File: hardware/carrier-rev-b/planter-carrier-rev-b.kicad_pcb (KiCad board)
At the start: 2 copper layers, 50.1 x 32.6 mm, 24 parts, among them J1 PROTECTED BATTERY, J2 MOISTURE PROBE, J3 WEACT 1.54 INCH, J4 XIAO BAT LEADS, Q1 AO3401A, U1 Seeed XIAO ESP32-C6 or ESP32-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

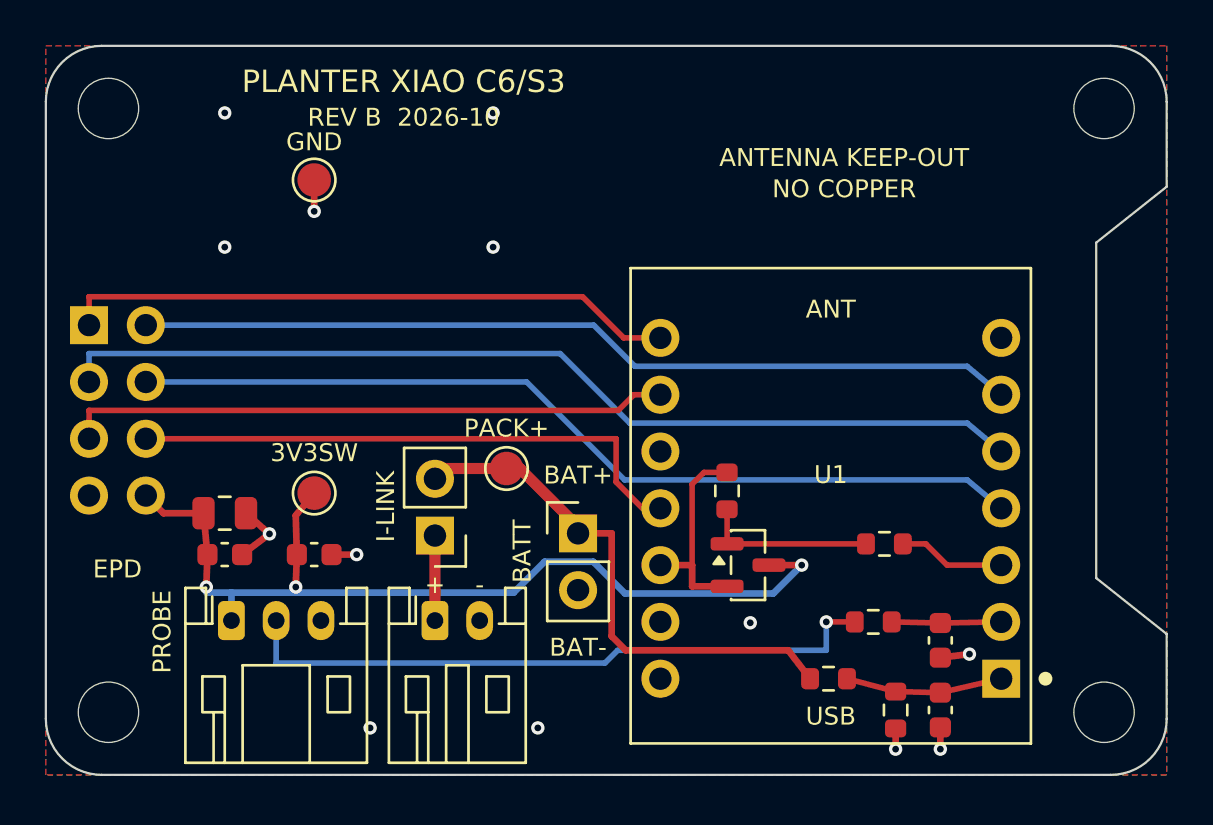
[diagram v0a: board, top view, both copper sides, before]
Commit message: Rev B carrier: freeze on XIAO ESP32-S3, soldered flat
The socketed C6-or-S3 layout left the XIAO's underside BAT pads to a
flying lead that had to leave the socket tunnel and loop back to J4, and
the module could only sit on headers above the passives. With one chip
the board can use its exact land pattern instead.

- U1 is Seeed's XIAO-ESP32-S3-SMD land pattern, rotated so USB-C stays
  at the bottom edge. The underside BAT+/BAT- pads land on plated pads
  (solder from the back, or reflow); J4 is gone.
- Nothing sits under the module. The S3 uses a U.FL antenna, so the C6
  antenna keep-out is dropped: the XIAO moves left beside J3 and the
  switch, divider and filters use the freed right side and top band.
- Pin map rearranged for the layout (display on the left-row pins, D6/TX
  unconnected); firmware Rev B map and platformio-rev-b.ini follow, and
  the C6 env is removed.
- Generators find KiCad on Linux as well as macOS. check.sh passes on
  KiCad 10.0.7: ERC, DRC and parity clean.

Co-Authored-By: Claude Opus 5.5 <noreply@anthropic.com>
Claude-Session: https://claude.ai/code/session_01Y2pFZDRMef9EECGaLGphfU
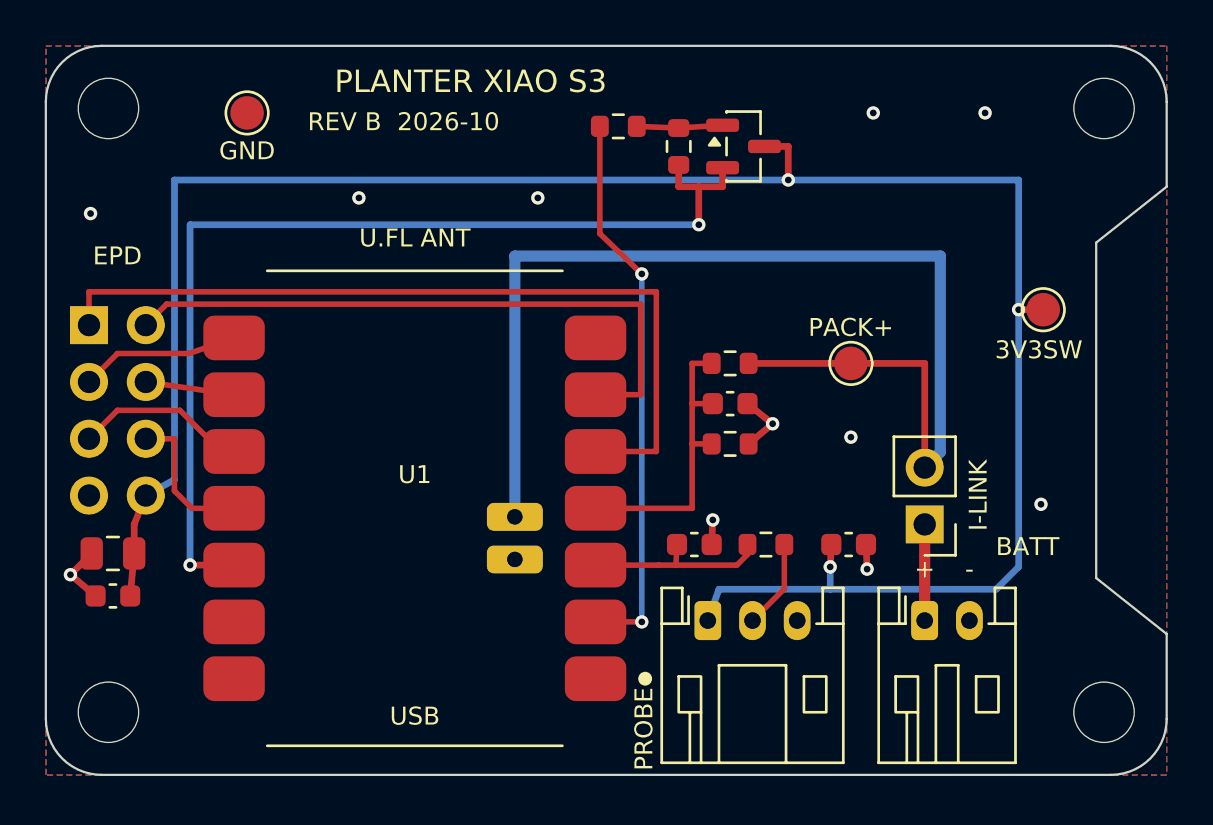
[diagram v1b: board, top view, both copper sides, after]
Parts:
- removed J4: XIAO BAT LEADS, Connector_PinHeader_2.54mm:PinHeader_1x02_P2.54mm_Vertical
- U1: value Seeed XIAO ESP32-C6 or ESP32-S3 -> Seeed XIAO ESP32-S3; footprint Planter:Seeed_XIAO_Socketed_2x7_P2.54mm -> Planter:Seeed_XIAO_ESP32S3_SMD
- moved TP3 33.6 mm to (144.6, 111.8)
- moved C5 23.9 mm to (135.9, 122.3)
- moved R4 22.1 mm to (125.6, 103.6), turned to 0 degrees
- moved JP1 21.9 mm to (139.3, 121.4)
- moved J1 21.9 mm to (139.3, 125.7)
- moved J2 21.3 mm to (129.6, 125.7)
- moved Q1 18.7 mm to (131.2, 104.5)
- moved U1 18.6 mm to (116.5, 120.7)
- moved C1 16.6 mm to (130.6, 116.0), turned to 0 degrees
- moved TP1 16.1 mm to (136.0, 114.2)
- moved R1 15.6 mm to (128.3, 104.5), turned to 90 degrees
- moved R2 14.8 mm to (130.6, 114.2), turned to 180 degrees
- moved R3 14.0 mm to (130.6, 117.8), turned to 0 degrees
- moved C4 11.8 mm to (129.0, 122.3), turned to 0 degrees
- moved R5 5.92 mm to (132.2, 122.3), turned to 180 degrees
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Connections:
- U1 pad 1: /VBAT_ADC -> unconnected-(U1-D0/A0_IO1-Pad1)
- U1 pad 10: unconnected-(U1-D9_C6:IO20_S3:IO8-Pad10) -> /EPD_SCLK
- U1 pad 2: /MOIST_ADC -> /PERIPH_EN_N
- U1 pad 3: /PERIPH_EN_N -> /MOIST_ADC
- U1 pad 4: /EPD_CS -> /VBAT_ADC
- U1 pad 5: /EPD_DC -> /EPD_BUSY
- U1 pad 8: /EPD_BUSY -> /EPD_DC
- U1 pad 9: /EPD_SCLK -> /EPD_CS
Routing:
- net /3V3_SW: track 41.7 -> 95.5 mm
- net /EPD_DC: track 43.8 -> 7.13 mm
- net /EPD_CS: track 40.5 -> 3.99 mm
- net /3V3: track 9.33 -> 45.4 mm, vias 0 -> 2
- net /PACK+: track 23.8 -> 53.0 mm
- net /MOIST_OUT: track 29.3 -> 3.99 mm, vias 1 -> 0
- net /PERIPH_EN_N: track 4.79 -> 25.0 mm, vias 0 -> 2
- net /EPD_SCLK: track 27.1 -> 7.78 mm
- net /EPD_MOSI: track 25.4 -> 6.60 mm
- net /EPD_RST: track 39.5 -> 28.6 mm
- net /EPD_BUSY: track 27.6 -> 36.7 mm
- net /VBAT_ADC: track 7.04 -> 13.5 mm
- net /GATE: track 7.76 -> 3.84 mm
- net /MOIST_ADC: track 4.90 -> 8.36 mm
- net /GND: track 8.67 -> 7.86 mm, vias 13 -> 11
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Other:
- board text added: "PLANTER XIAO S3"
- board text added: "SOLDER FROM HERE"
- board text added: "U.FL ANT"
- board text removed: "ANTENNA KEEP-OUT"
- board text removed: "NO COPPER"
- board text removed: "PLANTER XIAO C6/S3"

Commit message: Rev B: drop the BAT- pad; return through the GND castellation
The XIAO's underside BAT- pad is module GND, the same net as castellation
13, so a carrier pad under it only added a hidden joint 0.65 mm from BAT+
that could short the cell, and one that is hard to heat on the planes. It
now sits on solder mask and the battery returns through the GND
castellation.

README: the BAT+ pad is plated through, so a stencil puts no paste on it;
it is soldered from the back even when the rest is reflowed. Add a
TP1-to-GND short check and a powered check of the hidden joint.

Co-Authored-By: Claude Opus 5.5 <noreply@anthropic.com>
Claude-Session: https://claude.ai/code/session_01Y2pFZDRMef9EECGaLGphfU
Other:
- board text removed: "BAT-"
